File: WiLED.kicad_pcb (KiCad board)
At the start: 2 copper layers, 35 x 71.9 mm, 60 parts, among them J1 Mount, J2 Mount, J3 Mount, J4 Mount, P1 Serial to USB, P2 DC In, P4 LED Out, SW1 Reset, SW2 Boot, SW3 Toggle, SW4 Rotary Encoder, U1 ESP-WROOM-32, U2 TS3004x, U3 AL8860WT-7, U4 HC-SR501

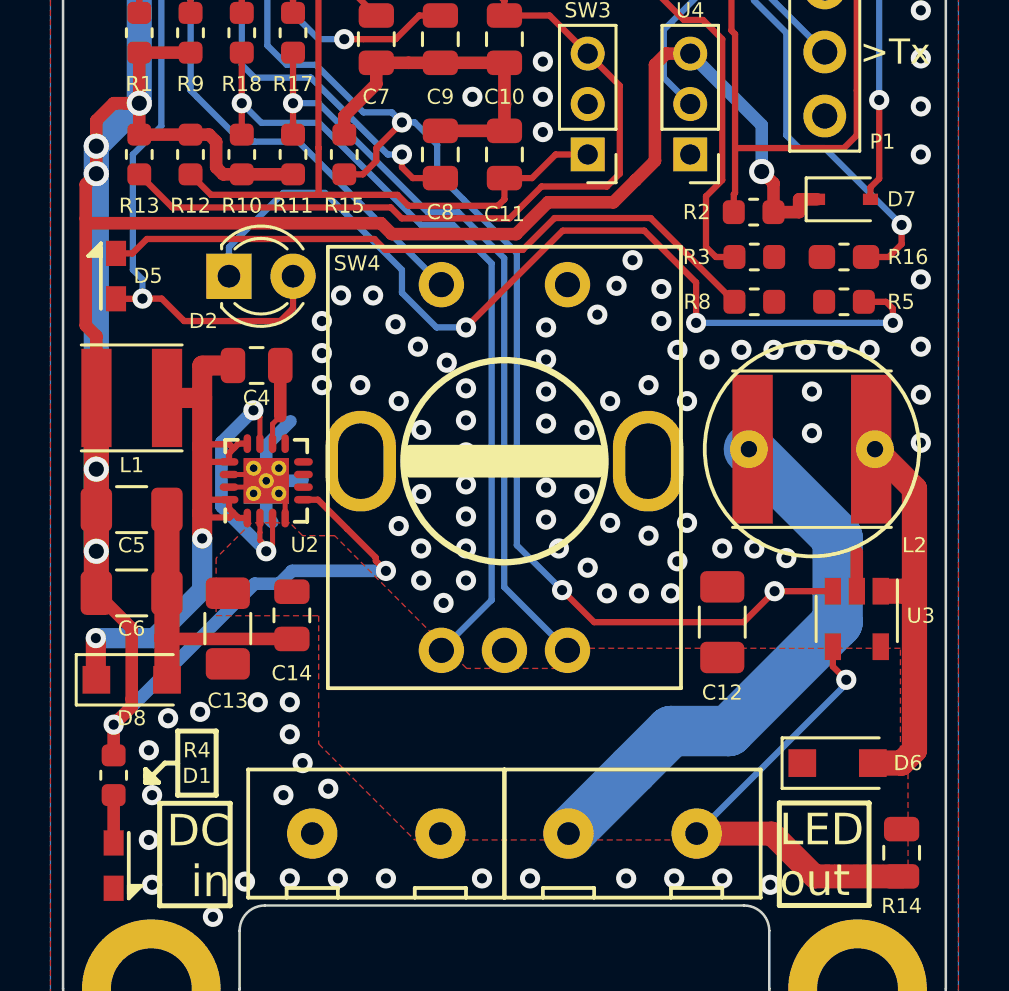
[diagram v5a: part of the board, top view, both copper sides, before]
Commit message: Move lower section components down slightly
There is still a little bit more tightening that can be done vertically
on the PCB layout. Some of the components on the lower part of the board
have been moved down, to make space to move other components into.
The PCB width is acceptable, but reducing the height would be ideal.
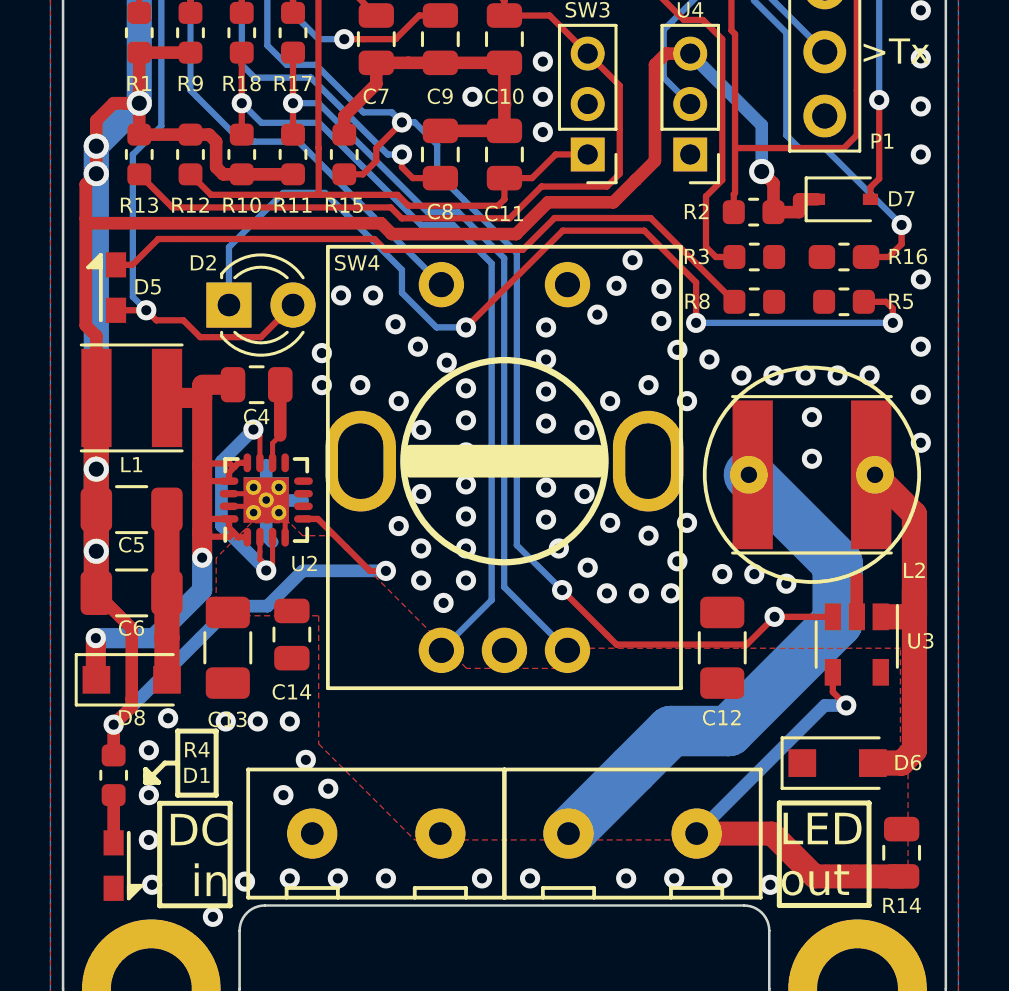
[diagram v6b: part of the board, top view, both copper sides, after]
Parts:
- moved D2 1.14 mm to (161.8, 103.8)
- moved C12 1.02 mm to (181.4, 117.3)
- moved U3 1.02 mm to (186.7, 117.2)
- moved L2 1.02 mm to (184.9, 110.5)
- moved REF** 1.02 mm to (184.9, 110.5)
- moved C13 0.76 mm to (161.8, 117.3)
- moved C14 0.76 mm to (164.3, 116.8)
- moved C4 0.76 mm to (162.9, 106.9)
- moved U2 0.76 mm to (163.3, 111.5)
- moved D5 0.45 mm to (157.3, 103.1)
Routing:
- net GND: track 40.0 -> 33.6 mm, vias 177 -> 175
- net Net-(D2-Pad1): track 37.0 -> 38.1 mm
- net LED_NEG: track 22.5 -> 21.4 mm
- net Net-(C4-Pad2): track 25.8 -> 25.1 mm

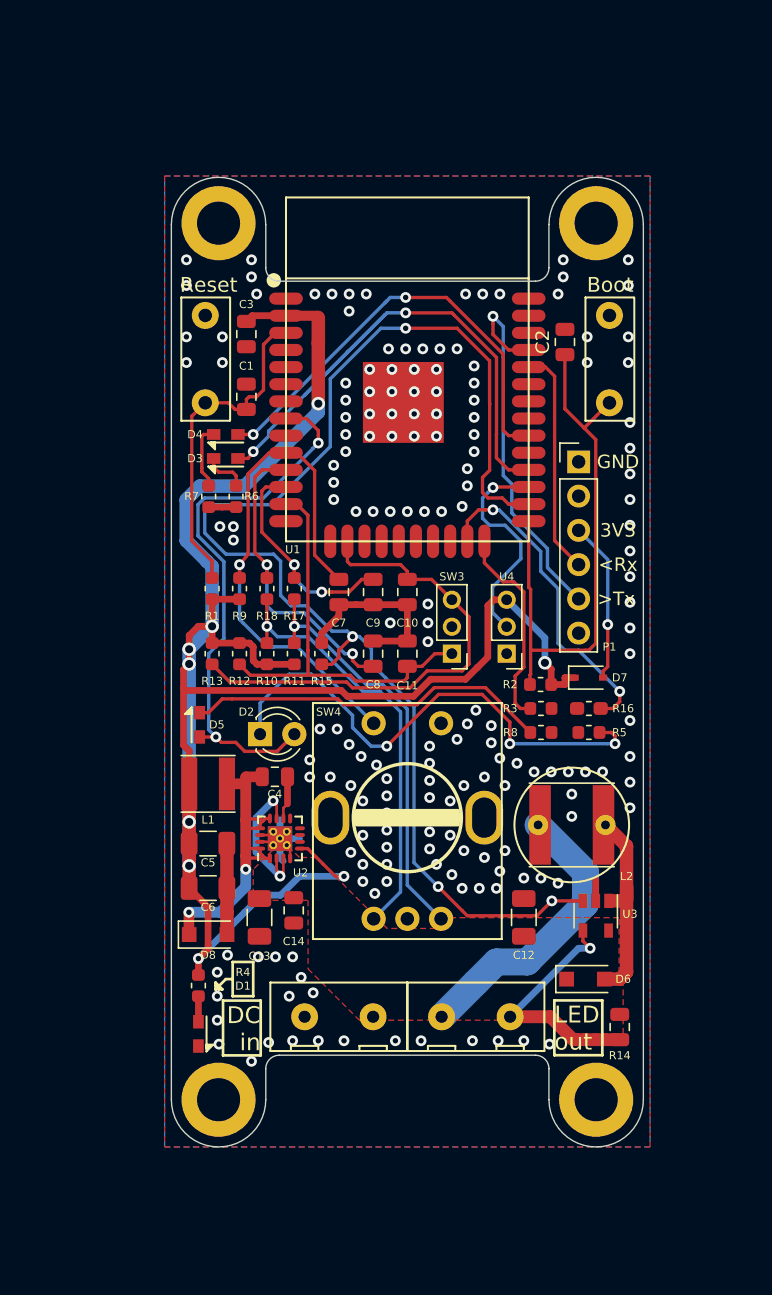
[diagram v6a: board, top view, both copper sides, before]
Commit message: Move top components down, shorten board height
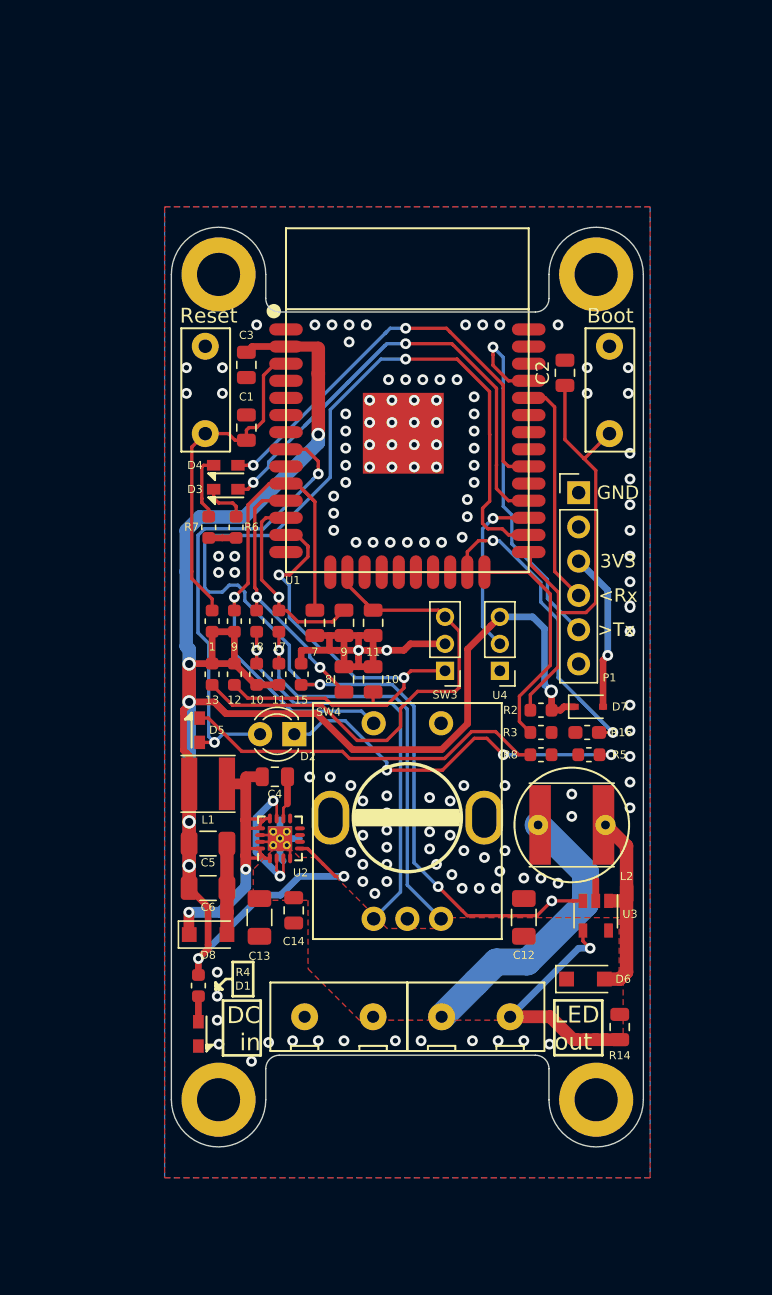
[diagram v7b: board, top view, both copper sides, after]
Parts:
- removed R9: 10k, Resistor_SMD:R_0603_1608Metric
- added 9: 10k, Resistor_SMD:R_0603_1608Metric, F.Cu at (159.9, 95.4)
- moved J1 3.80 mm to (158.7, 69.7)
- moved J2 3.80 mm to (186.7, 69.7)
- moved 11 3.42 mm to (170.2, 95.5)
- moved 10 3.17 mm to (170.2, 99.7)
- moved 9 3.14 mm to (168.0, 95.5)
- moved 7 2.90 mm to (165.9, 95.5)
- moved 8 2.88 mm to (168.0, 99.7)
- moved 17 2.67 mm to (163.2, 95.4)
- moved D2 2.54 mm to (164.3, 103.8), turned to 180 degrees
- moved 18 2.53 mm to (161.5, 95.4)
- moved 1 2.41 mm to (158.2, 95.4)
- moved C1 2.29 mm to (160.8, 81.0)
- moved C2 2.29 mm to (184.4, 77.0)
- moved C3 2.29 mm to (160.8, 76.4)
- moved D3 2.29 mm to (159.3, 85.6)
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- renumbered R1 to 1, C10 to 10, R10 to 10, C11 to 11, R11 to 11, R12 to 12, R13 to 13, R15 to 15, R17 to 17, R18 to 18, C7 to 7, C8 to 8, C9 to 9
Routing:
- net GND: track 33.6 -> 46.2 mm, vias 175 -> 136
- net Net-(D2-Pad1): track 38.1 -> 28.8 mm
- net TGL_1: track 31.4 -> 38.2 mm, vias 0 -> 2
- net IND_PWM: track 41.9 -> 35.3 mm
- net IO0: track 42.3 -> 36.3 mm
- net PIR_TRG: track 16.5 -> 12.8 mm
- net ENC_A: track 25.0 -> 21.5 mm
- net ENC_B: track 17.9 -> 15.4 mm, vias 2 -> 1
- net LED_PWM: track 99.0 -> 96.6 mm
- net Net-(R16-Pad1): track 24.4 -> 26.5 mm
- net +3V3: track 151.1 -> 149.1 mm, vias 9 -> 8
- net IO2: track 15.2 -> 17.1 mm
- net TGL_2: track 36.6 -> 37.3 mm
- net CON_B: track 30.9 -> 31.6 mm
- net ENC_SW: track 40.4 -> 41.0 mm
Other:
- board size 35 x 71.9 mm -> 35 x 68.2 mm

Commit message: Re-do layout, for v3.0
Having started the 3D CAD for the enclosure, it seems that the PCB is
able to be slightly wider than previously planned. To make the most of
this new width, a complete rearrange has been done - the PCB is now a
square shape.
Routing has been completed on this new layout, vias still need to be
added.
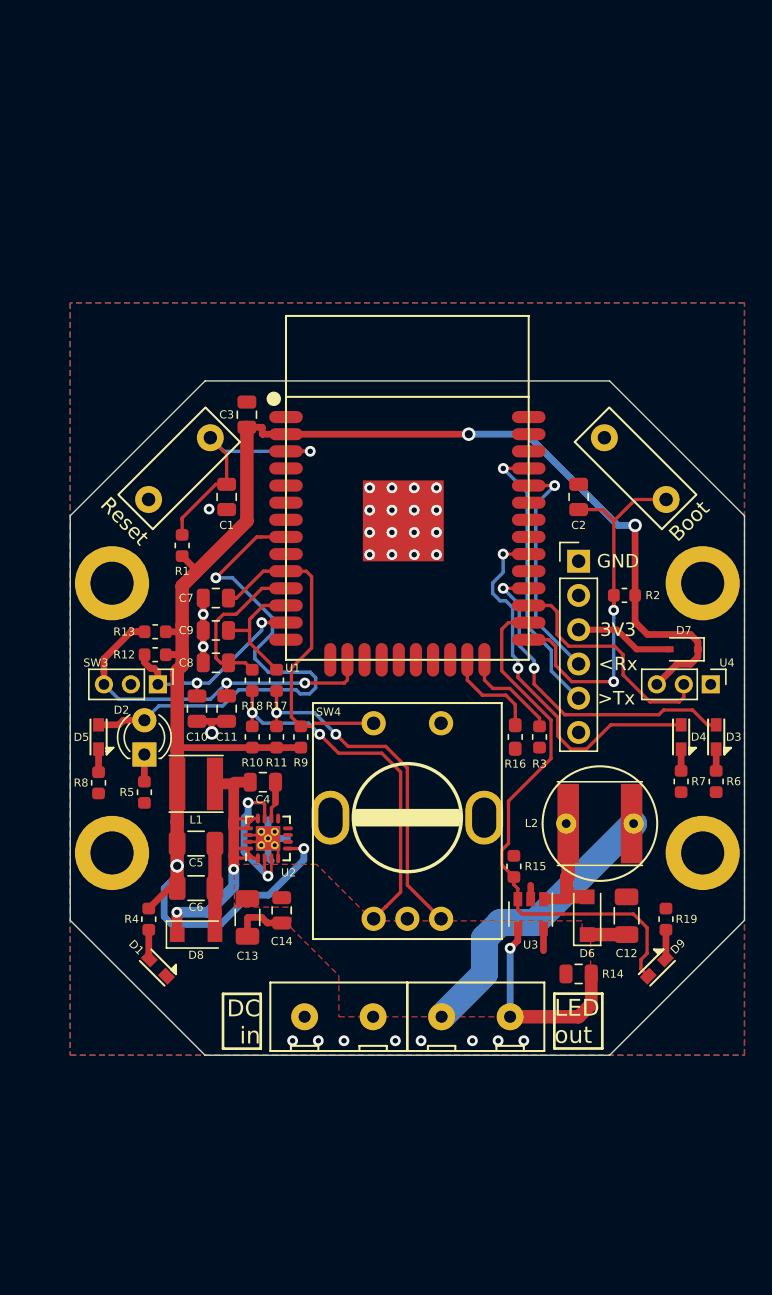
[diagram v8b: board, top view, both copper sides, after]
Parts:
- removed 1, 10, 11, 12, 13, 15, 17, 18, 9: 10k, Resistor_SMD:R_0603_1608Metric
- removed 10, 11, 7, 8, 9: 100nF, Capacitor_SMD:C_0805_2012Metric
- added C10: 100nF, Capacitor_SMD:C_0805_2012Metric, F.Cu at (157.1, 101.9)
- added C11: 100nF, Capacitor_SMD:C_0805_2012Metric, F.Cu at (159.3, 101.9)
- added C7: 100nF, Capacitor_SMD:C_0805_2012Metric, F.Cu at (158.5, 93.7)
- added C8: 100nF, Capacitor_SMD:C_0805_2012Metric, F.Cu at (158.5, 98.5)
- added C9: 100nF, Capacitor_SMD:C_0805_2012Metric, F.Cu at (158.5, 96.1)
- added D9: PWM LED, custom-footprints:WL-SMCW, F.Cu at (191.2, 121.1)
- added R1: 10k, Resistor_SMD:R_0603_1608Metric, F.Cu at (156.0, 89.8)
- added R10: 10k, Resistor_SMD:R_0603_1608Metric, F.Cu at (161.2, 104.0)
- added R11: 10k, Resistor_SMD:R_0603_1608Metric, F.Cu at (163.0, 104.0)
- added R12: 10k, Resistor_SMD:R_0603_1608Metric, F.Cu at (154.0, 97.9)
- added R13: 10k, Resistor_SMD:R_0603_1608Metric, F.Cu at (154.0, 96.2)
- added R15: 10k, Resistor_SMD:R_0603_1608Metric, F.Cu at (180.6, 113.6)
- added R17: 10k, Resistor_SMD:R_0603_1608Metric, F.Cu at (163.0, 99.8)
- added R18: 10k, Resistor_SMD:R_0603_1608Metric, F.Cu at (161.2, 99.8)
- added R19: 1k, Resistor_SMD:R_0603_1608Metric, F.Cu at (191.9, 117.5)
- added R9: 10k, Resistor_SMD:R_0603_1608Metric, F.Cu at (164.8, 104.0)
- moved D3 40.7 mm to (195.6, 104.0), turned to 90 degrees
- moved R6 40.3 mm to (195.6, 107.3)
- moved R7 39.8 mm to (193.0, 107.3)
- moved D4 39.3 mm to (193.0, 104.0), turned to 90 degrees
- moved R5 33.1 mm to (153.2, 108.1), turned to 90 degrees
- moved R8 32.9 mm to (149.8, 107.4), turned to 90 degrees
- moved J1 24.2 mm to (150.8, 92.6)
- moved J2 24.2 mm to (194.6, 92.6)
- moved SW3 21.3 mm to (154.2, 100.1), turned to 270 degrees
- moved J3 19.9 mm to (150.8, 112.6)
- moved J4 19.9 mm to (194.6, 112.6)
- moved U4 15.7 mm to (195.2, 100.1), turned to 270 degrees
- moved D2 11.2 mm to (153.2, 105.3), turned to 90 degrees
- moved R2 10.5 mm to (188.8, 93.5)
- moved C2 9.26 mm to (185.4, 86.2)
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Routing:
- net LED_PWM: track 96.6 -> 40.7 mm, vias 4 -> 0
- net +3V3: track 149.1 -> 120.2 mm, vias 8 -> 4
- net Net-(D2-Pad1): track 28.8 -> 2.01 mm, vias 3 -> 0
- net Net-(D5-Pad1): track 27.3 -> 1.71 mm
- net TGL_1: track 38.2 -> 15.5 mm
- net IO17: track 44.4 -> 25.0 mm
- net Net-(R16-Pad1): track 26.5 -> 7.33 mm, vias 2 -> 0
- net GND: track 46.2 -> 29.4 mm, vias 136 -> 28
- net ENC_SW: track 41.0 -> 24.7 mm, vias 1 -> 0
- net TGL_2: track 37.3 -> 27.3 mm, vias 0 -> 2
- net IO2: track 17.1 -> 7.37 mm
- net ENC_A: track 21.5 -> 12.0 mm, vias 2 -> 0
- net IO0: track 36.3 -> 28.9 mm, vias 0 -> 2
- net TX: track 28.1 -> 21.2 mm
- net Net-(D6-Pad2): track 15.4 -> 8.79 mm
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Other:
- board size 35 x 68.2 mm -> 50 x 50 mm
- net class POWER: trace_width 0.5 -> 0.25
- board text added: "v3.0 Main Board"
- board text removed: "v2.1 Main Board"
